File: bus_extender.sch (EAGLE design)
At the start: 6 parts, among them CON1 CON-4P-TABS-JST_GH-RA, CON2 CON-4P-TABS-JST_GH-RA

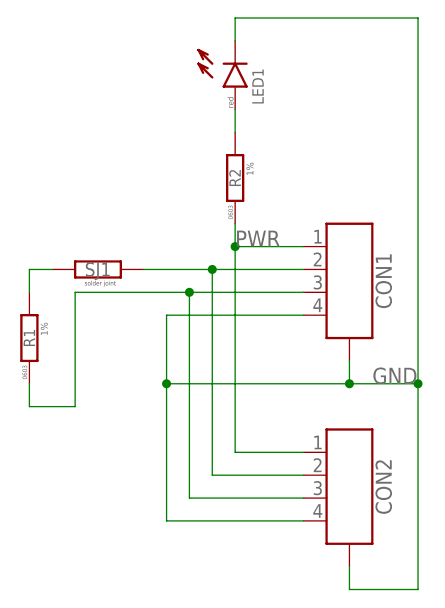
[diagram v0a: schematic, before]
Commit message: Added part numbers for R1, R2, and LED1 (#1)
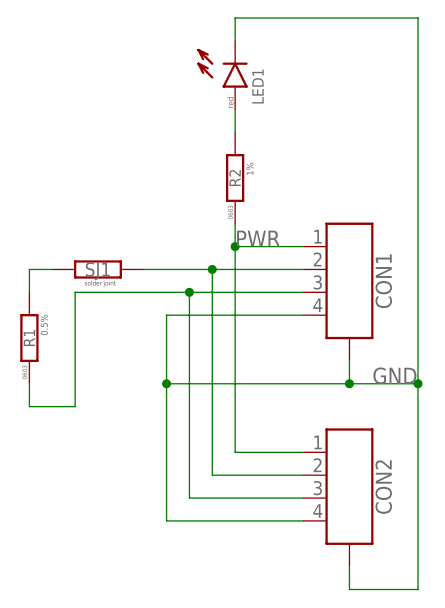
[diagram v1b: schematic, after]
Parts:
- LED1: DIGIKEY# (none) -> 511-1587-1-ND; MANF (none) -> Rohm Semiconductor; MANF# (none) -> SML-E12V8WT86
- R1: DIGIKEY# (none) -> 311-121DCT-ND; MANF (none) -> YAGEO; MANF# (none) -> RT0603DRD07121RL; OPERATING_TEMP (none) -> -55°C ~ 155°C; TOLERANCE (none) -> 0.5%
- R2: DIGIKEY# (none) -> RHM200ADCT-ND; MANF (none) -> Rohm Semiconductor; MANF# (none) -> ESR03EZPF2000; OPERATING_TEMP (none) -> -55°C ~ 155°C
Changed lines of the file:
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@@
 <?xml version="1.0" encoding="utf-8"?>
 <!DOCTYPE eagle SYSTEM "eagle.dtd">
-<eagle version="9.6.1">
+<eagle version="9.6.2">
 <drawing>
 <settings>
@@
 <part name="CON1" library="Connectors" library_urn="urn:adsk.eagle:library:3750510" deviceset="CON-4P-TABS" device="-RA" package3d_urn="urn:adsk.eagle:package:1040150/6" technology="-JST_GH"/>
 <part name="CON2" library="Connectors" library_urn="urn:adsk.eagle:library:3750510" deviceset="CON-4P-TABS" device="-RA" package3d_urn="urn:adsk.eagle:package:1040150/6" technology="-JST_GH"/>
-<part name="R1" library="rc" library_urn="urn:adsk.eagle:library:2539423" deviceset="R" device="-0603" package3d_urn="urn:adsk.eagle:package:2539454/2" technology="-1%"/>
+<part name="R1" library="rc" library_urn="urn:adsk.eagle:library:2539423" deviceset="R" device="-0603" package3d_urn="urn:adsk.eagle:package:2539454/2" technology="-1%">
+<attribute name="DIGIKEY#" value="311-121DCT-ND"/>
+<attribute name="MANF" value="YAGEO"/>
+<attribute name="MANF#" value="RT0603DRD07121RL"/>
+<attribute name="OPERATING_TEMP" value="-55°C ~ 155°C"/>
+<attribute name="TOLERANCE" value="0.5%"/>
+</part>
 <part name="SJ1" library="misc" library_urn="urn:adsk.eagle:library:5347860" deviceset="SOLDER_JOINT" device="" package3d_urn="urn:adsk.eagle:package:20998874/1"/>
 <part name="LED1" library="rc" library_urn="urn:adsk.eagle:library:2539423" deviceset="LED" device="-0603" package3d_urn="urn:adsk.eagle:package:2539471/2">
 <attribute name="COLOR" value="red"/>
+<attribute name="DIGIKEY#" value="511-1587-1-ND"/>
+<attribute name="MANF" value="Rohm Semiconductor"/>
+<attribute name="MANF#" value="SML-E12V8WT86"/>
 </part>
-<part name="R2" library="rc" library_urn="urn:adsk.eagle:library:2539423" deviceset="R" device="-0603" package3d_urn="urn:adsk.eagle:package:2539454/2" technology="-1%"/>
+<part name="R2" library="rc" library_urn="urn:adsk.eagle:library:2539423" deviceset="R" device="-0603" package3d_urn="urn:adsk.eagle:package:2539454/2" technology="-1%">
+<attribute name="DIGIKEY#" value="RHM200ADCT-ND"/>
+<attribute name="MANF" value="Rohm Semiconductor"/>
+<attribute name="MANF#" value="ESR03EZPF2000"/>
+<attribute name="OPERATING_TEMP" value="-55°C ~ 155°C"/>
+</part>
 </parts>
 <sheets>
